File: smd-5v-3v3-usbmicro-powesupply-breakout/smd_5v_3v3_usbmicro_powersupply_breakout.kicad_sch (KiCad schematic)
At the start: 11 parts, among them J1 USB_B_Micro, J2 SMD Pads, J3 THT Pins, U1 LMS1585AIS-3.3

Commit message: Update tvs diode
- Actually picked a part rather than a placeholder one
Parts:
- D1: value PTVS5V0Z1USKP -> ESDB5V0WT; footprint Diode_SMD:Nexperia_DSN1608-2_1.6x0.8mm -> Diode_SMD:D_SOD-523; MPN (none) -> ESDB5V0WT
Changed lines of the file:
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@@
 			)
 		)
-		(property "Value" "PTVS5V0Z1USKP"
-			(at 39.116 54.102 0)
+		(property "Value" "ESDB5V0WT"
+			(at 39.116 56.642 0)
 			(effects
 				(font
@@
 			)
 		)
-		(property "Footprint" "Diode_SMD:Nexperia_DSN1608-2_1.6x0.8mm"
+		(property "Footprint" "Diode_SMD:D_SOD-523"
 			(at 37.465 60.96 0)
 			(effects
@@
 			)
 		)
-		(property "Datasheet" "https://assets.nexperia.com/documents/data-sheet/PTVS5V0Z1USKP.pdf"
+		(property "Datasheet" ""
 			(at 41.91 60.96 0)
 			(effects
@@
 			)
 		)
-		(property "Description" "5V, 2000W TVS unidirectional diode, DSN1608-2"
+		(property "Description" "5V TVS unidirectional diode"
 			(at 41.91 60.96 0)
 			(effects
+				(font
+					(size 1.27 1.27)
+				)
+				(hide yes)
+			)
+		)
+		(property "MPN" "ESDB5V0WT"
+			(at 41.91 60.96 0)
+			(effects

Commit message: Update ferrite bead (schematic)
- 2220 imperial SMD package size seems to have a decent amount of
  components currently available for a wide range of impedances
- TI SPRAAR7A doc suggests a ferribe bead between 47 and 1000 ohms rated
  at 100MHz with the ferrite bead continuing to be resistive at 1GHz
- Seen various different rated ferrite beads on VBUS line which supports
  the above claim
- Therefore chose a 300R component for now with the possibilty of
  changing it out to a ~100R or 600R ferrite bead if the desired
  filtering isn't achieved
- Capacitive 2220 footprint chosen as ferrite bead isn't polarised
  therefore is the same footprint as a capacitor (no KiCad SMD 2220
  inductor footprint exists either)
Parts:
- FB1: value 30R @ 100 MHz -> 300R @ 100 MHz; footprint Inductor_SMD:L_0603_1608Metric -> Capacitor_SMD:C_2220_5750Metric_Pad1.97x5.40mm_HandSolder; MPN (none) -> HI2220R301R-10
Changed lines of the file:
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@@
 			)
 		)
-		(property "Value" "30R @ 100 MHz"
+		(property "Value" "300R @ 100 MHz"
 			(at 79.9592 46.99 90)
 			(effects
@@
 			)
 		)
-		(property "Footprint" "Inductor_SMD:L_0603_1608Metric"
+		(property "Footprint" "Capacitor_SMD:C_2220_5750Metric_Pad1.97x5.40mm_HandSolder"
 			(at 80.01 53.848 90)
 			(effects
@@
 			(at 80.01 52.07 0)
 			(effects
+				(font
+					(size 1.27 1.27)
+				)
+				(hide yes)
+			)
+		)
+		(property "MPN" "HI2220R301R-10"
+			(at 80.01 52.07 0)
+			(effects

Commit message: Add part number for usb b micro connector
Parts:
- J1: MPN (none) -> 10118194-0001LF
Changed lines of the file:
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@@
+			)
+		)
+		(property "MPN" " 10118194-0001LF"
+			(at 57.15 69.85 0)
+			(effects
+				(font
+					(size 1.27 1.27)
+				)
+				(hide yes)
 			)
 		)

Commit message: Exclude smd pads from bom
- They are just exposed copper, no need for them to be on the BOM
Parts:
- J2: now left out of the parts list
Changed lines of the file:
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@@
 		(unit 1)
 		(exclude_from_sim no)
-		(in_bom yes)
+		(in_bom no)
 		(on_board yes)
 		(dnp no)

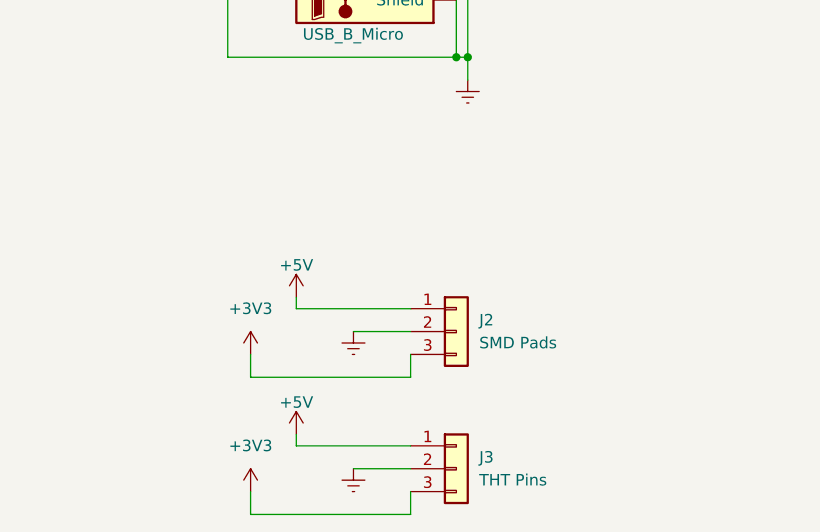
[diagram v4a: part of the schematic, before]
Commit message: Update schematic and pcb
- Having the 3 pin connectors was awkward, split them up into two
  separate connectors for each power plane
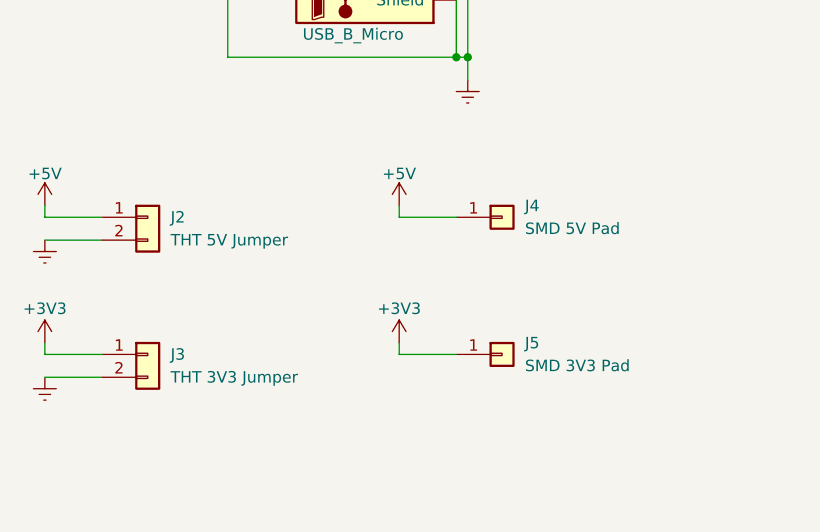
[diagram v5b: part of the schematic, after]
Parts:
- removed J2: SMD Pads, Connector_PinHeader_1.00mm:PinHeader_1x03_P1.00mm_Vertical_SMD_Pin1Right, symbol Connector_Generic:Conn_01x03
- removed J3: THT Pins, Connector_PinHeader_1.00mm:PinHeader_1x03_P1.00mm_Vertical, symbol Connector_Generic:Conn_01x03
- added J2: THT 5V Jumper, Connector_PinHeader_2.54mm:PinHeader_1x02_P2.54mm_Vertical, symbol Connector_Generic:Conn_01x02
- added J3: THT 3V3 Jumper, Connector_PinHeader_2.54mm:PinHeader_1x02_P2.54mm_Vertical, symbol Connector_Generic:Conn_01x02
- added J4: SMD 5V Pad, Connector_Wire:SolderWirePad_1x01_SMD_5x10mm, symbol Connector_Generic:Conn_01x01
- added J5: SMD 3V3 Pad, Connector_Wire:SolderWirePad_1x01_SMD_5x10mm, symbol Connector_Generic:Conn_01x01
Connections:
- net +3V3: now also J3.1 (Pin_1), J5.1 (Pin_1)
- net +5V: now also J2.1 (Pin_1), J4.1 (Pin_1)
- net GND: now also J2.2 (Pin_2), J3.2 (Pin_2)
